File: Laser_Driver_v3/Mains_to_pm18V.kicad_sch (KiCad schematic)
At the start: 24 parts, among them Q1 Q_NMOS_DGS IRF530, Q2 Q_PMOS_DGS IRF9530, T1 Transformer_1P_SS

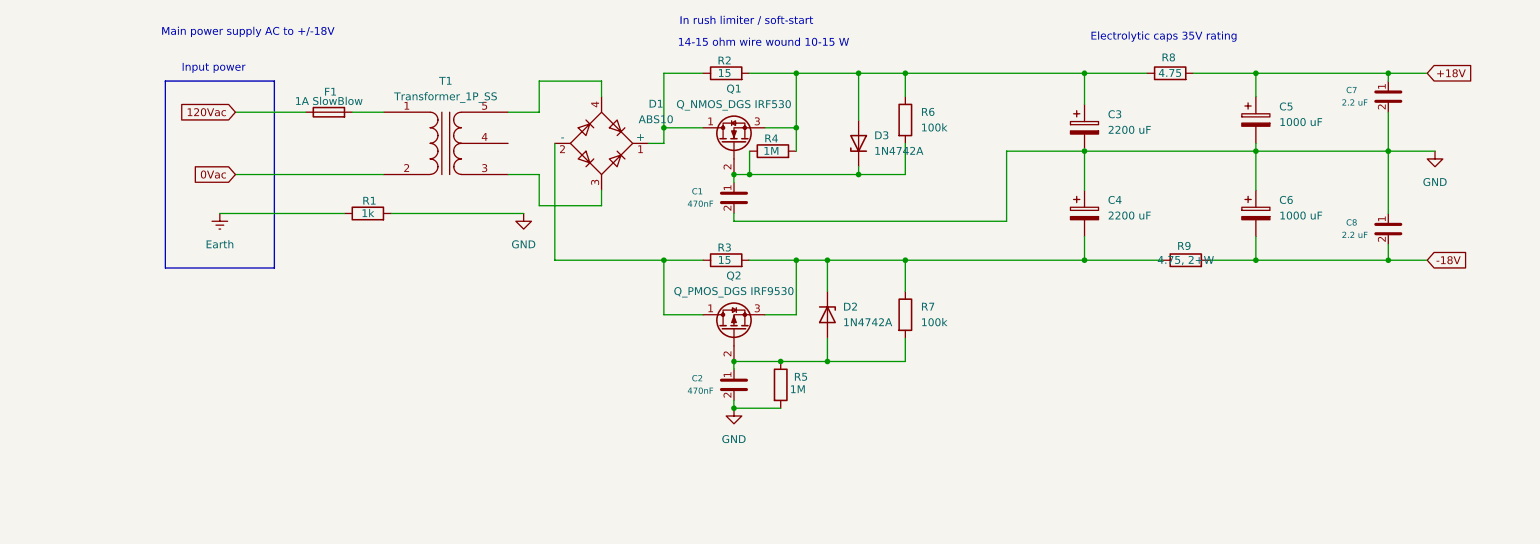
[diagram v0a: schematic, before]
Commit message: Update names, footprints, values, and created BOM
Updated files names, foot prints, component values, parts.
Assigned values from Digikey catalog.
Created CSV BOMs for each schematic.
Including a Power analysis now for all components.
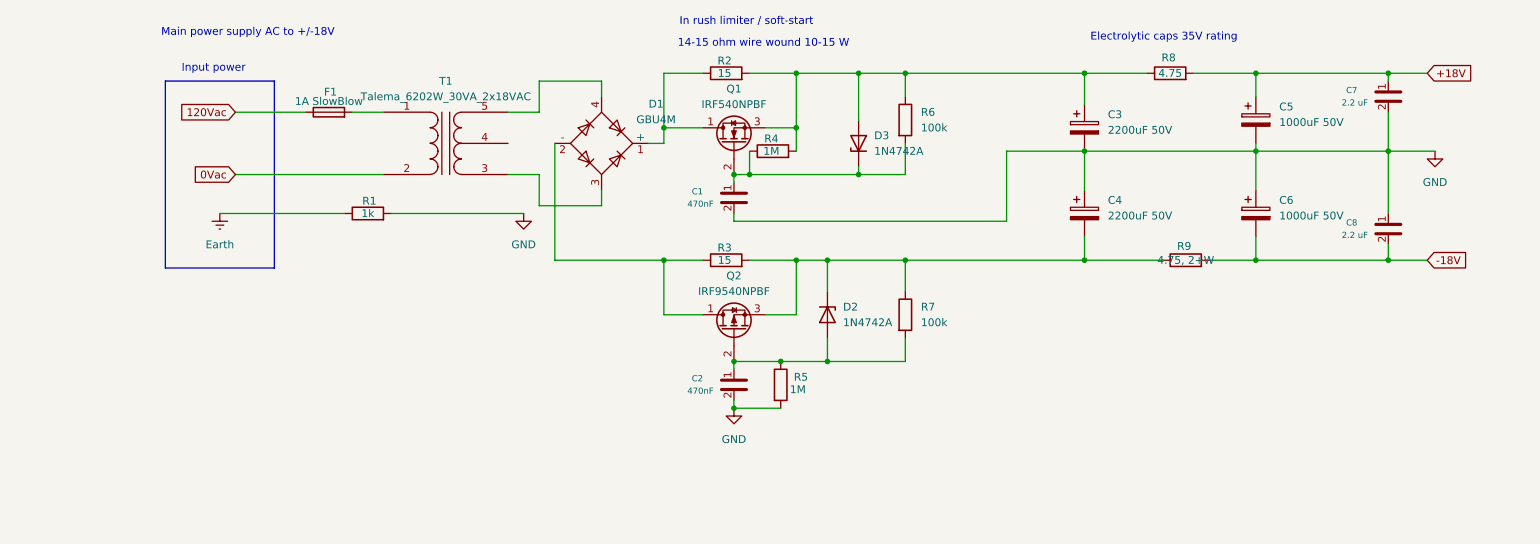
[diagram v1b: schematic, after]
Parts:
- C3, C4: value 2200 uF -> 2200uF 50V; footprint (none) -> Capacitor_THT:CP_Radial_D18.0mm_P7.50mm
- C5, C6: value 1000 uF -> 1000uF 50V; footprint (none) -> Capacitor_THT:CP_Radial_D16.0mm_P7.50mm
- D1: value ABS10 -> GBU4M; footprint Diode_SMD:Diode_Bridge_Diotec_ABS -> Diode_THT:Diode_Bridge_Inline_4Leads_WOM-4.8x6.8mm_P2.54mm
- Q1: value Q_NMOS_DGS IRF530 -> IRF540NPBF; footprint (none) -> Package_TO_SOT_THT:TO-220-3_Vertical
- Q2: value Q_PMOS_DGS IRF9530 -> IRF9540NPBF; footprint (none) -> Package_TO_SOT_THT:TO-220-3_Vertical
- T1: value Transformer_1P_SS -> Talema_6202W_30VA_2x18VAC
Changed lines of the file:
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@@
 			)
 		)
-		(property "Value" "Q_NMOS_DGS IRF530"
+		(property "Value" "IRF540NPBF"
 			(at 134.62 57.15 90)
 			(show_name no)
@@
 			)
 		)
-		(property "Footprint" ""
+		(property "Footprint" "Package_TO_SOT_THT:TO-220-3_Vertical"
 			(at 132.08 58.42 0)
 			(hide yes)
@@
 			)
 		)
-		(property "Value" "2200 uF"
+		(property "Value" "2200uF 50V"
 			(at 195.58 75.3109 0)
 			(show_name no)
@@
 			)
 		)
-		(property "Footprint" ""
+		(property "Footprint" "Capacitor_THT:CP_Radial_D18.0mm_P7.50mm"
 			(at 192.7352 78.74 0)
 			(hide yes)
@@
 			)
 		)
-		(property "Value" "1000 uF"
+		(property "Value" "1000uF 50V"
 			(at 223.52 60.0709 0)
 			(show_name no)
@@
 			)
 		)
-		(property "Footprint" ""
+		(property "Footprint" "Capacitor_THT:CP_Radial_D16.0mm_P7.50mm"
 			(at 220.6752 63.5 0)
 			(hide yes)
@@
 			)
 		)
-		(property "Value" "1000 uF"
+		(property "Value" "1000uF 50V"
 			(at 223.52 75.3109 0)
 			(show_name no)
@@
 			)
 		)
-		(property "Footprint" ""
+		(property "Footprint" "Capacitor_THT:CP_Radial_D16.0mm_P7.50mm"
 			(at 220.6752 78.74 0)
 			(hide yes)
@@
 			)
 		)
-		(property "Value" "2200 uF"
+		(property "Value" "2200uF 50V"
 			(at 195.58 61.3409 0)
 			(show_name no)
@@
 			)
 		)
-		(property "Footprint" ""
+		(property "Footprint" "Capacitor_THT:CP_Radial_D18.0mm_P7.50mm"
 			(at 192.7352 64.77 0)
 			(hide yes)
@@
 			)
 		)
-		(property "Value" "ABS10"
+		(property "Value" "GBU4M"
 			(at 121.92 59.6198 0)
 			(show_name no)
@@
 			)
 		)
-		(property "Footprint" "Diode_SMD:Diode_Bridge_Diotec_ABS"
+		(property "Footprint" "Diode_THT:Diode_Bridge_Inline_4Leads_WOM-4.8x6.8mm_P2.54mm"
 			(at 116.84 60.325 0)
 			(hide yes)
@@
 			)
 		)
-		(property "Value" "Transformer_1P_SS"
+		(property "Value" "Talema_6202W_30VA_2x18VAC"
 			(at 87.6427 55.88 0)
 			(show_name no)
@@
 			)
 		)
-		(property "Value" "Q_PMOS_DGS IRF9530"
+		(property "Value" "IRF9540NPBF"
 			(at 134.62 87.63 90)
 			(show_name no)
@@
 			)
 		)
-		(property "Footprint" ""
+		(property "Footprint" "Package_TO_SOT_THT:TO-220-3_Vertical"
 			(at 132.08 88.9 0)
 			(hide yes)

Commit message: Clearing ERC errors. laying out components.
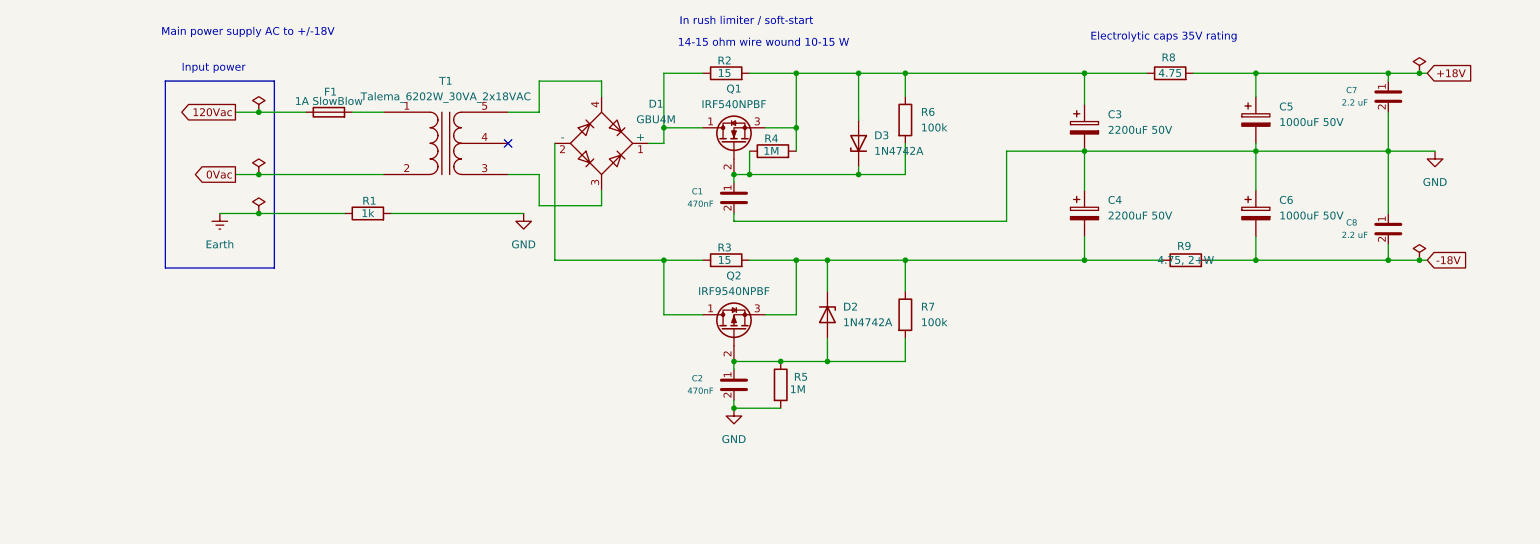
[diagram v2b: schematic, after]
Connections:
- no-connect marks 0 -> 1

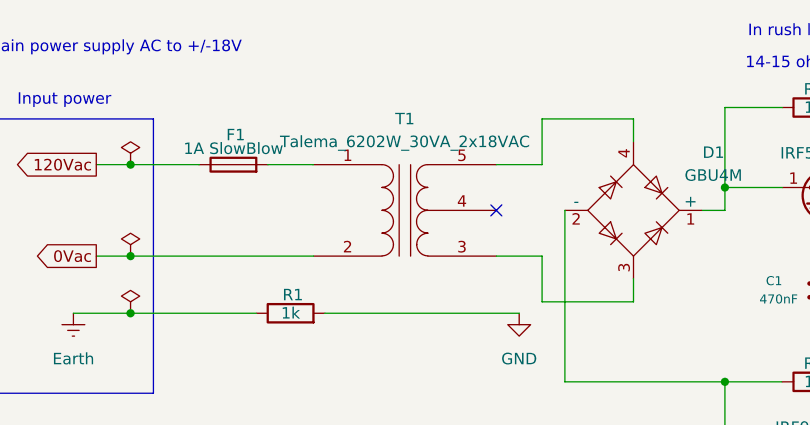
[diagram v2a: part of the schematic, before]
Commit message: Added display to schematic.  Updated BOM.
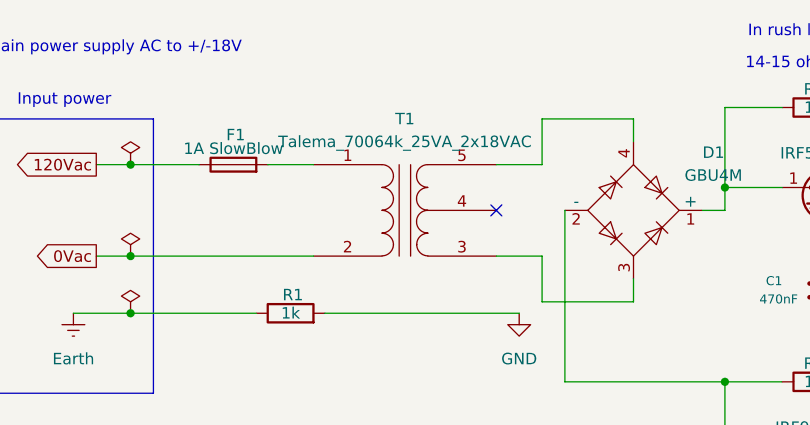
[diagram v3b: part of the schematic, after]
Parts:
- R1, R4, R5, R6, R8: footprint (none) -> Resistor_SMD:R_0805_2012Metric_Pad1.20x1.40mm_HandSolder
- R9: footprint (none) -> Resistor_SMD:R_2512_6332Metric_Pad1.40x3.35mm_HandSolder
- T1: value Talema_6202W_30VA_2x18VAC -> Talema_70064k_25VA_2x18VAC
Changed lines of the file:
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@@
 			)
 		)
-		(property "Footprint" ""
+		(property "Footprint" "Resistor_SMD:R_0805_2012Metric_Pad1.20x1.40mm_HandSolder"
 			(at 74.93 76.708 90)
 			(hide yes)
@@
 			)
 		)
-		(property "Footprint" ""
+		(property "Footprint" "Resistor_SMD:R_2512_6332Metric_Pad1.40x3.35mm_HandSolder"
 			(at 208.28 84.328 90)
 			(hide yes)
@@
 			)
 		)
-		(property "Footprint" ""
+		(property "Footprint" "Resistor_SMD:R_0805_2012Metric_Pad1.20x1.40mm_HandSolder"
 			(at 160.782 59.69 90)
 			(hide yes)
@@
 			)
 		)
-		(property "Footprint" ""
+		(property "Footprint" "Resistor_SMD:R_0805_2012Metric_Pad1.20x1.40mm_HandSolder"
 			(at 205.74 53.848 90)
 			(hide yes)
@@
 			)
 		)
-		(property "Footprint" ""
+		(property "Footprint" "Resistor_SMD:R_0805_2012Metric_Pad1.20x1.40mm_HandSolder"
 			(at 140.462 102.87 90)
 			(hide yes)
@@
 			)
 		)
-		(property "Footprint" ""
+		(property "Footprint" "Resistor_SMD:R_0805_2012Metric_Pad1.20x1.40mm_HandSolder"
 			(at 140.97 66.548 90)
 			(hide yes)
@@
 			)
 		)
-		(property "Value" "Talema_6202W_30VA_2x18VAC"
+		(property "Value" "Talema_70064k_25VA_2x18VAC"
 			(at 87.6427 55.88 0)
 			(show_name no)

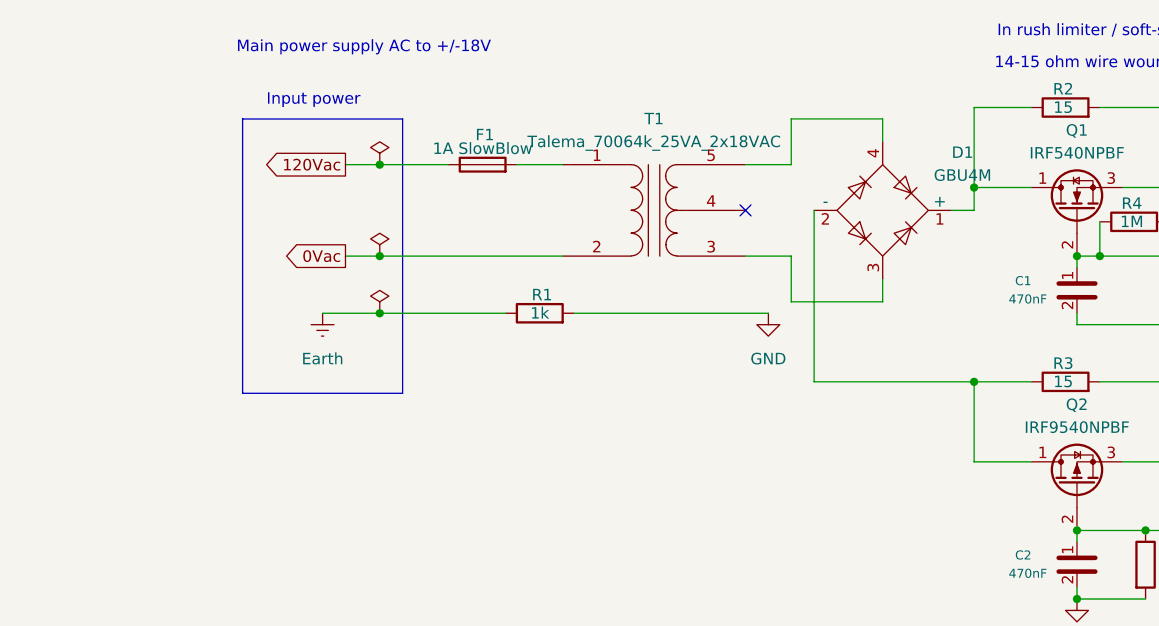
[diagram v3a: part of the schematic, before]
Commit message: Update to teensy pinout and config. Working on PCB
Improved pin selection on Teensy for better operation.
Started working through the PCB from in the power input.
Updating footprints and getting the layout organized.
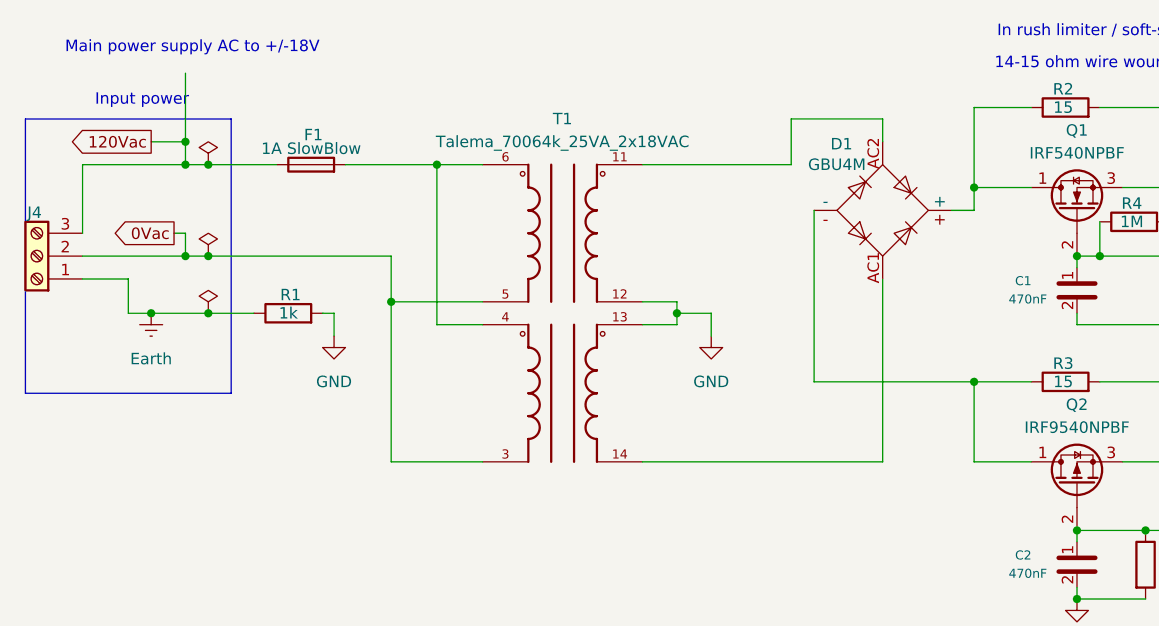
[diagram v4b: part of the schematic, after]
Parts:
- added J4: Screw_Terminal_01x03, symbol Connector:Screw_Terminal_01x03
- D1: footprint Diode_THT:Diode_Bridge_Inline_4Leads_WOM-4.8x6.8mm_P2.54mm -> Diode_THT:Diode_Bridge_Vishay_GBU; symbol Diode_Bridge:ABS10 -> Diode_Bridge:GBU4M
- R8: footprint Resistor_SMD:R_0805_2012Metric_Pad1.20x1.40mm_HandSolder -> Resistor_SMD:R_2512_6332Metric_Pad1.40x3.35mm_HandSolder
- T1: footprint (none) -> Talema7006x:XFMR_70060K; symbol Device:Transformer_1P_SS -> 70060K:70060K; Availability (none) -> In Stock; Check_prices (none) -> https://www.snapeda.com/parts/70060K/Talema+Group+LLC/view-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; MF (none) -> Talema Group; MP (none) -> 70060K; PARTREV (none) -> N/A; Package (none) -> None; Price (none) -> None; STANDARD (none) -> Manufacturer Recommendations; SnapEDA_Link (none) -> https://www.snapeda.com/parts/70060K/Talema+Group+LLC/view-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
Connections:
- net 0Vac: now also T1.3, T1.5, J4.2 (Pin_2); no longer T1.2 (AB)
- net 120Vac: now also J4.3 (Pin_3)
- net Earth: now also J4.1 (Pin_1)
- net GND: now also T1.12, T1.13
- net at Q1.1 (D), R2.1: now also D1.+; no longer D1.1 (+)
- net at F1.2: now also T1.4, T1.6; no longer T1.1 (AA)
- net at Q2.1 (D), R3.1: now also D1.-; no longer D1.2 (-)
- new net: D1.AC1, T1.14
- new net: D1.AC2, T1.11
- no-connect marks 1 -> 0
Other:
- moved on the sheet: F1, R1

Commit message: Working through power supply layout and footprints
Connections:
- net at Q1.1 (D), R2.1: now also D1.1 (+); no longer D1.+
- net at Q2.1 (D), R3.1: now also D1.4 (-); no longer D1.-
- net at T1.14: now also D1.3; no longer D1.AC1
- net at T1.11: now also D1.2; no longer D1.AC2
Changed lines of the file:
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@@
 			)
 		)
-		(pin "AC2"
+		(pin "3"
 		)
-		(pin "AC1"
+		(pin "1"
 		)
-		(pin "-"
+		(pin "2"
 		)
-		(pin "+"
+		(pin "4"
 		)
 		(instances

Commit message: Began routing.
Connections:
- net -18V: now also D1.3, T1.14
- net +23V: now reaches D1.1 (+), Q1.1 (D), R2.1
- net +18VNF: now reaches C3.1, D3.2 (A), Q1.3 (S), R2.2, R4.2, R6.1, R8.1
- net -18VNF: now reaches C4.2, D2.1 (K), Q2.3 (S), R3.2, R7.1, R9.1
- net -23V: now reaches D1.4 (-), Q2.1 (D), R3.1
- net +18Vac: now reaches D1.2, T1.11
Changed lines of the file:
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@@
+		)
+	)
+	(label "-23V"
+		(at 118.11 82.55 0)
+		(effects
+			(font
+				(size 1.27 1.27)
+			)
+			(justify left bottom)
+		)
+	)
+	(label "-18V"
+		(at 101.6 91.44 0)
+		(effects
+			(font
+				(size 1.27 1.27)
+			)
+			(justify left bottom)
+		)
+	)
+	(label "+23V"
+		(at 123.19 52.07 0)
+		(effects
+			(font
+				(size 1.27 1.27)
+			)
+			(justify left bottom)
+		)
+	)
+	(label "+18Vac"
+		(at 106.68 53.34 0)
+		(effects
+			(font
+				(size 1.27 1.27)
+			)
+			(justify left bottom)
+		)
+	)
+	(label "-18VNF"
+		(at 167.64 82.55 0)
+		(effects
+			(font
+				(size 1.27 1.27)
+			)
+			(justify left bottom)
+		)
+	)
+	(label "+18VNF"
+		(at 173.99 52.07 0)
+		(effects
+			(font
+				(size 1.27 1.27)
+			)
+			(justify left bottom)
 		)
 	)

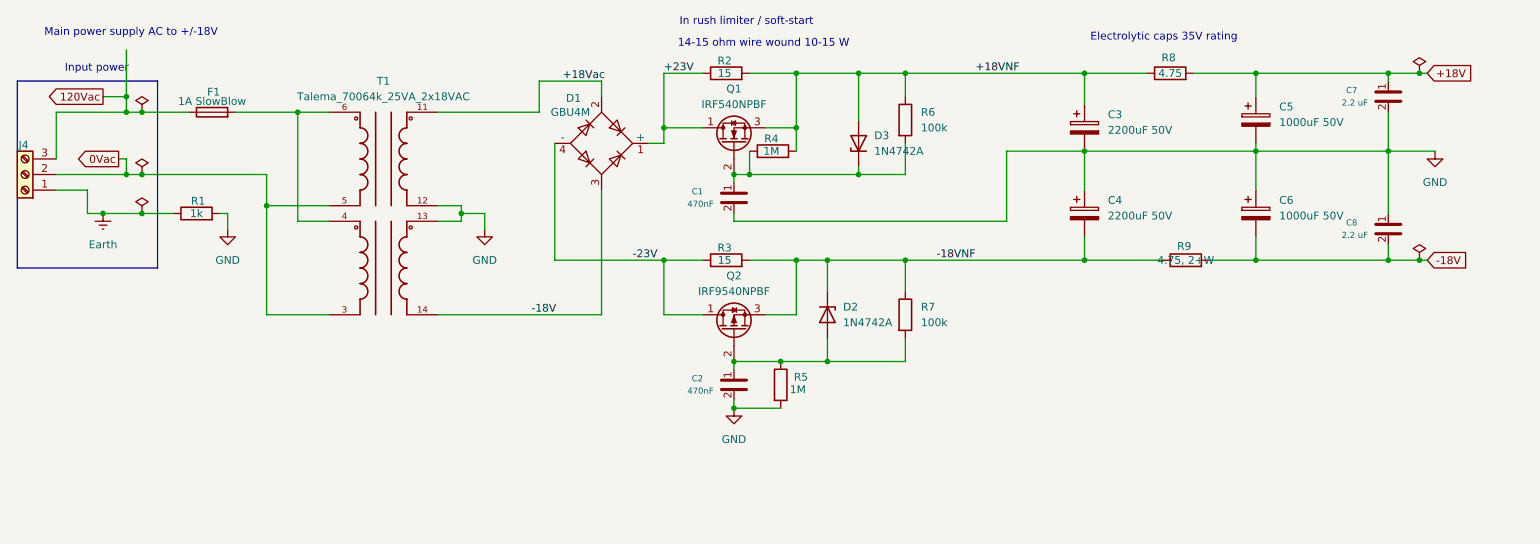
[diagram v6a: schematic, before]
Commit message: Added separate xfrmer for 6V.
Added inrush protection with NTC and increased capacitance to reduce ripple on 6V
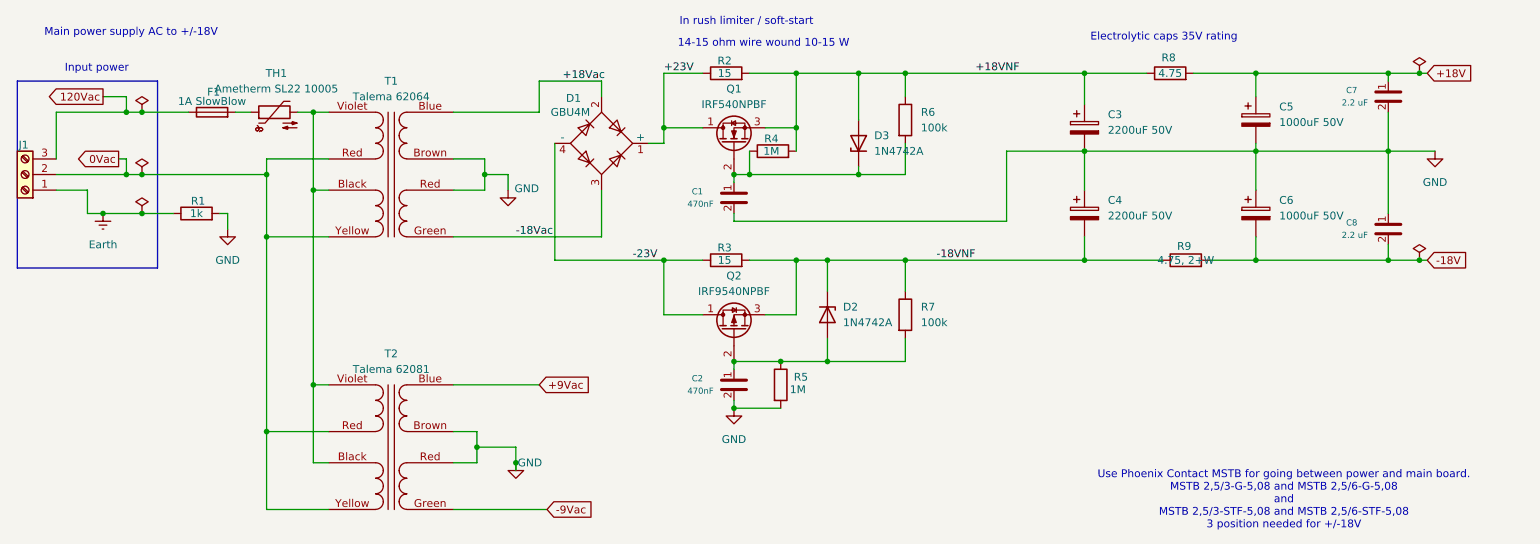
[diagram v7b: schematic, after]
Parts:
- removed T1: Talema_70064k_25VA_2x18VAC, Talema7006x:XFMR_70060K, symbol 70060K:70060K
- added T1: Talema 62064, symbol Device:Transformer_SP_2S
- added T2: Talema 62081, symbol Device:Transformer_SP_2S
- added TH1: Ametherm SL22 10005, Resistor_THT:R_Axial_DIN0411_L9.9mm_D3.6mm_P7.62mm_Vertical, symbol Device:Thermistor_NTC
- renumbered J4 to J1
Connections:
- net +18Vac: now also T1.Blue (-9V)
- net -18V: no longer D1.3
- net 0Vac: now also T1.Red (0V), T1.Yellow (0V), T2.Red (0V), T2.Yellow (0V)
- net GND: now also T1.Brown (0V), T1.Red (0V), T2.Brown (0V), T2.Red (0V)
- net at F1.2: now also TH1.1
- new net: T1.Black (115V), T1.Violet (115V), T2.Black (115V), T2.Violet (115V), TH1.2
- new net +9Vac: T2.Blue (-9V)
- new net -18Vac: D1.3, T1.Green (+9V)
- new net -9Vac: T2.Green (+9V)
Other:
- note added: "Use Phoenix Contact MSTB for going between power and main board. MSTB 2,5/3-G-5,08 and MSTB 2,5/6-G-5,08 and MSTB 2,5/3-STF-5,08 and MSTB 2,5/6-STF-5,08 3 position needed for +/-18V"
